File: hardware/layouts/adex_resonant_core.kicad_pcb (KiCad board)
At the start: 4 copper layers, 50 x 50 mm, 96 parts

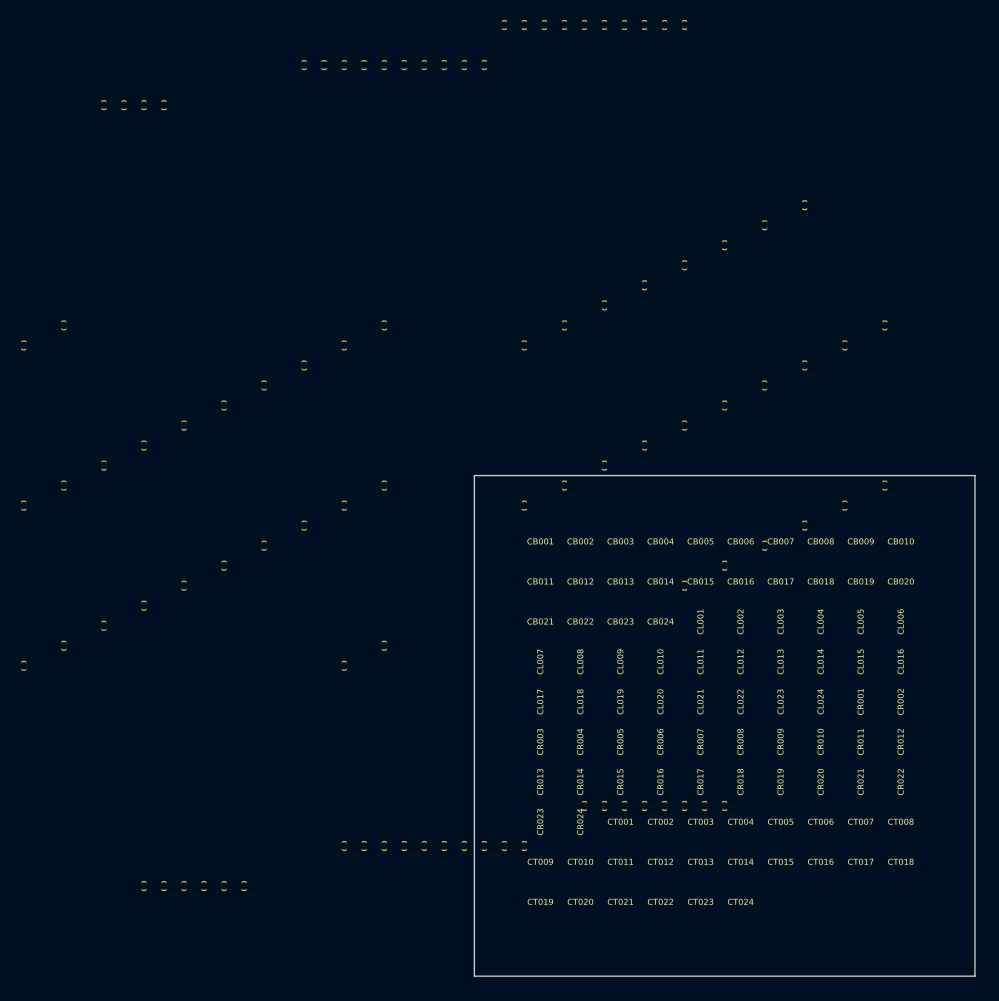
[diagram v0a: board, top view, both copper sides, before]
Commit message: fix(hardware): anchor castellated connectors to board edges and align inner SMD grid
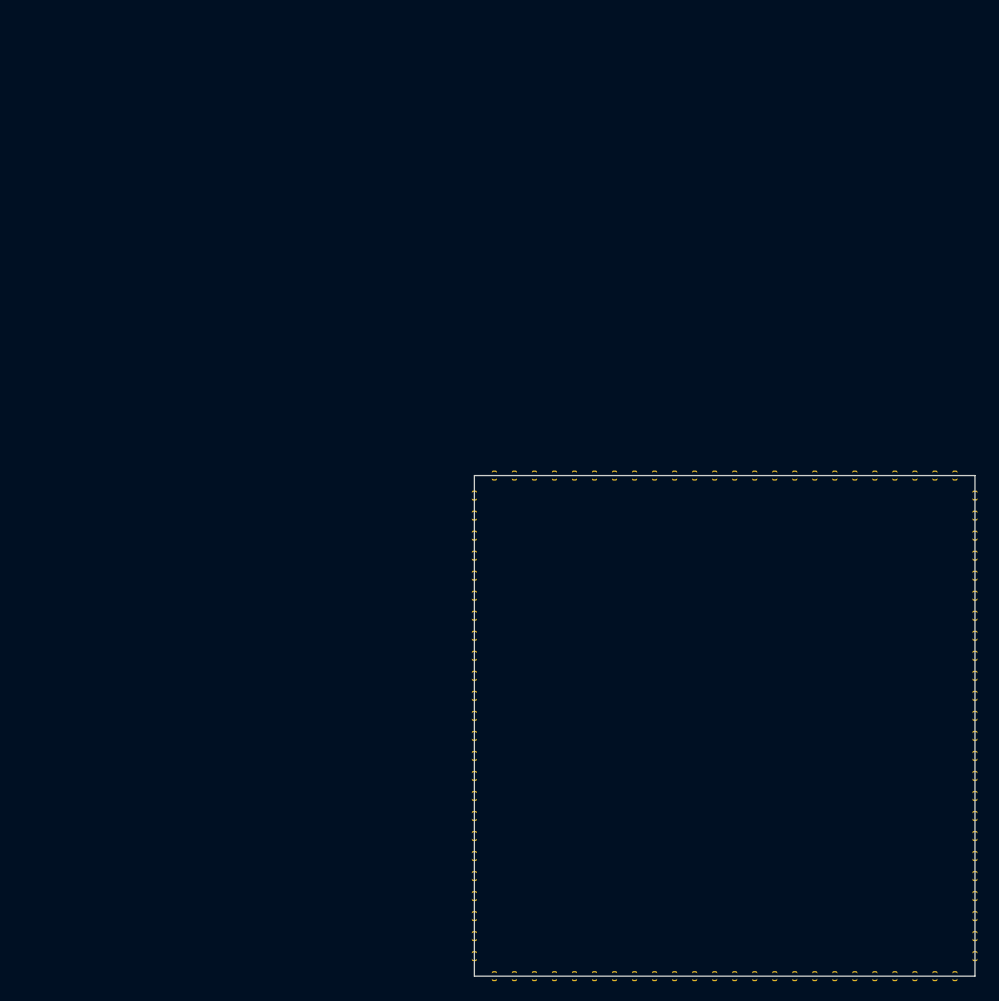
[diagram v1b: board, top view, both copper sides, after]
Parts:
- moved CT019 52.6 mm to (38.0, 0.00)
- moved CB021 52.3 mm to (42.0, 50.0)
- moved CT020 51.4 mm to (40.0, 0.00)
- moved CB022 50.9 mm to (44.0, 50.0)
- moved CT021 50.2 mm to (42.0, 0.00)
- moved CB010 49.7 mm to (20.0, 50.0)
- moved CB023 49.6 mm to (46.0, 50.0)
- moved CT022 49.1 mm to (44.0, 0.00)
- moved CB009 48.8 mm to (18.0, 50.0)
- moved CR003 48.8 mm to (50.0, 6.00)
- moved CB024 48.3 mm to (48.0, 50.0)
- moved CB008 48.1 mm to (16.0, 50.0)
- moved CT023 48.0 mm to (46.0, 0.00)
- moved CB007 47.4 mm to (14.0, 50.0)
- moved CT024 47.0 mm to (48.0, 0.00)
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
